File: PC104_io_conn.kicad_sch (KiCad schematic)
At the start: 8 parts, among them J1 ESQ-126-39-G-D, J2 ESQ-126-39-G-D

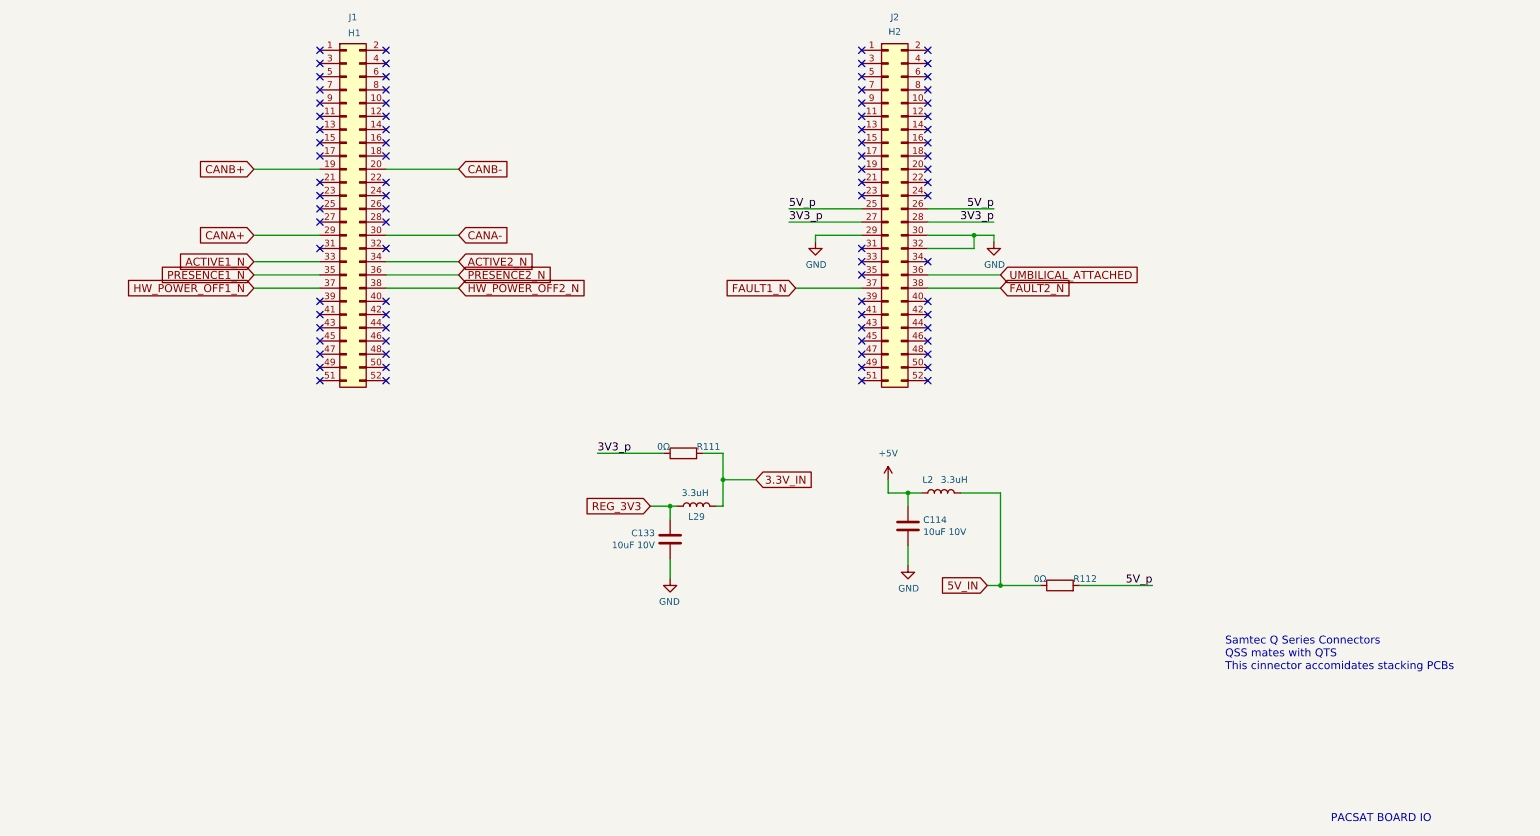
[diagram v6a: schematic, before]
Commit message: Add Power System Adapter function to the board
Signed-off-by: Corey Minyard <corey@minyard.net>
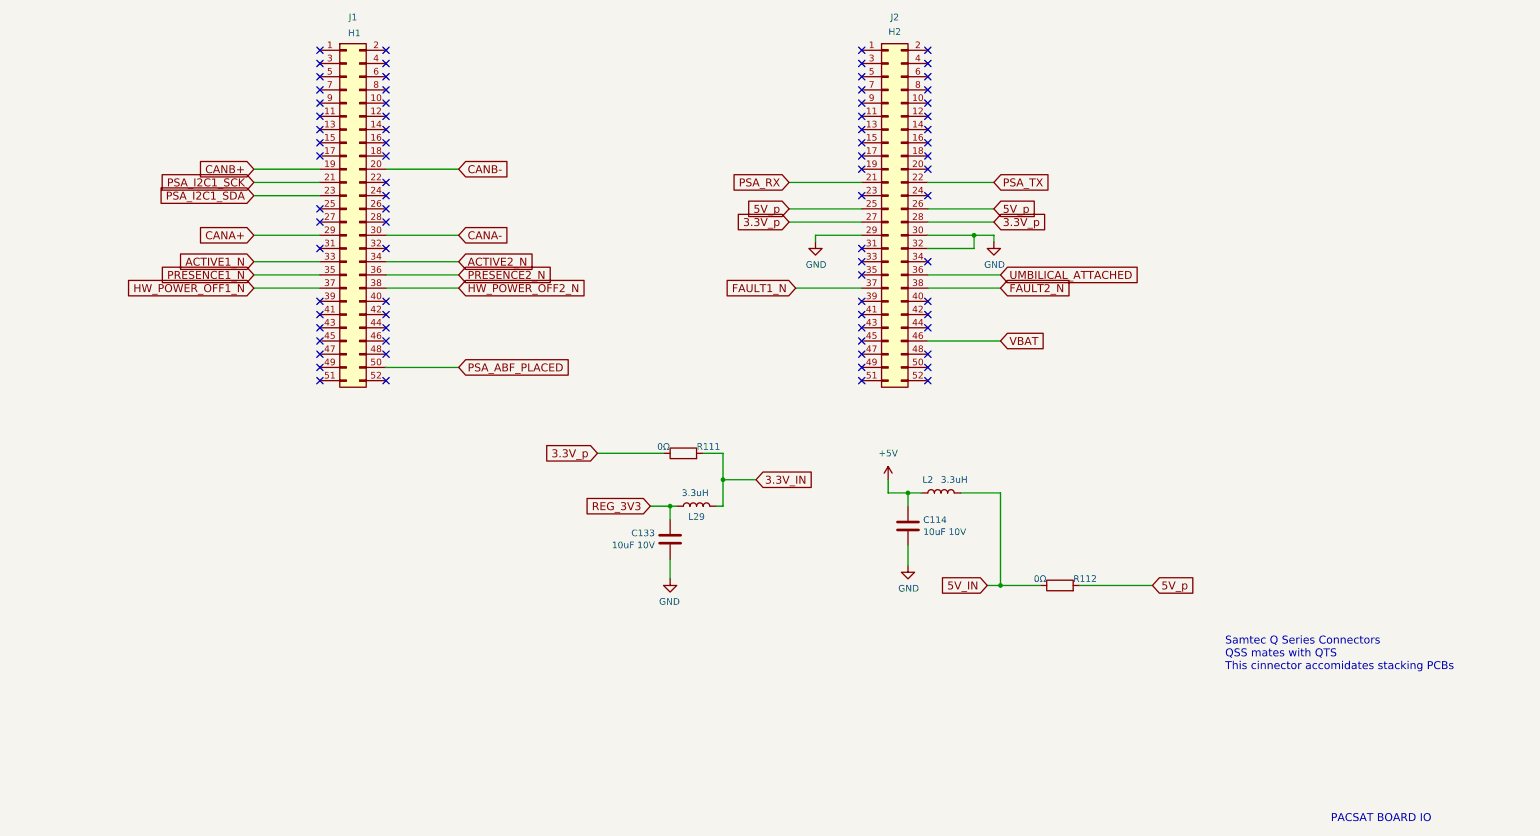
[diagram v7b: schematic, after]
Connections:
- net PSA_I2C1_SCK: now reaches J1.21 (Pin_21)
- net PSA_I2C1_SDA: now reaches J1.23 (Pin_23)
- net PSA_ABF_PLACED: now reaches J1.50 (Pin_50)
- net PSA_RX: now reaches J2.21 (Pin_21)
- net PSA_TX: now reaches J2.22 (Pin_22)
- net VBAT: now reaches J2.46 (Pin_46)
- net 3V3_p renamed 3.3V_p
- no-connect marks 84 -> 78

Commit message: Update the location and add a CSKB light connection
Move UMBILICAL_ATTACHED to the CSKB lite area, and add a SAFE\_MODE
pin to trigger the processor from another board to go into safe mode.

Signed-off-by: Corey Minyard <corey@minyard.net>
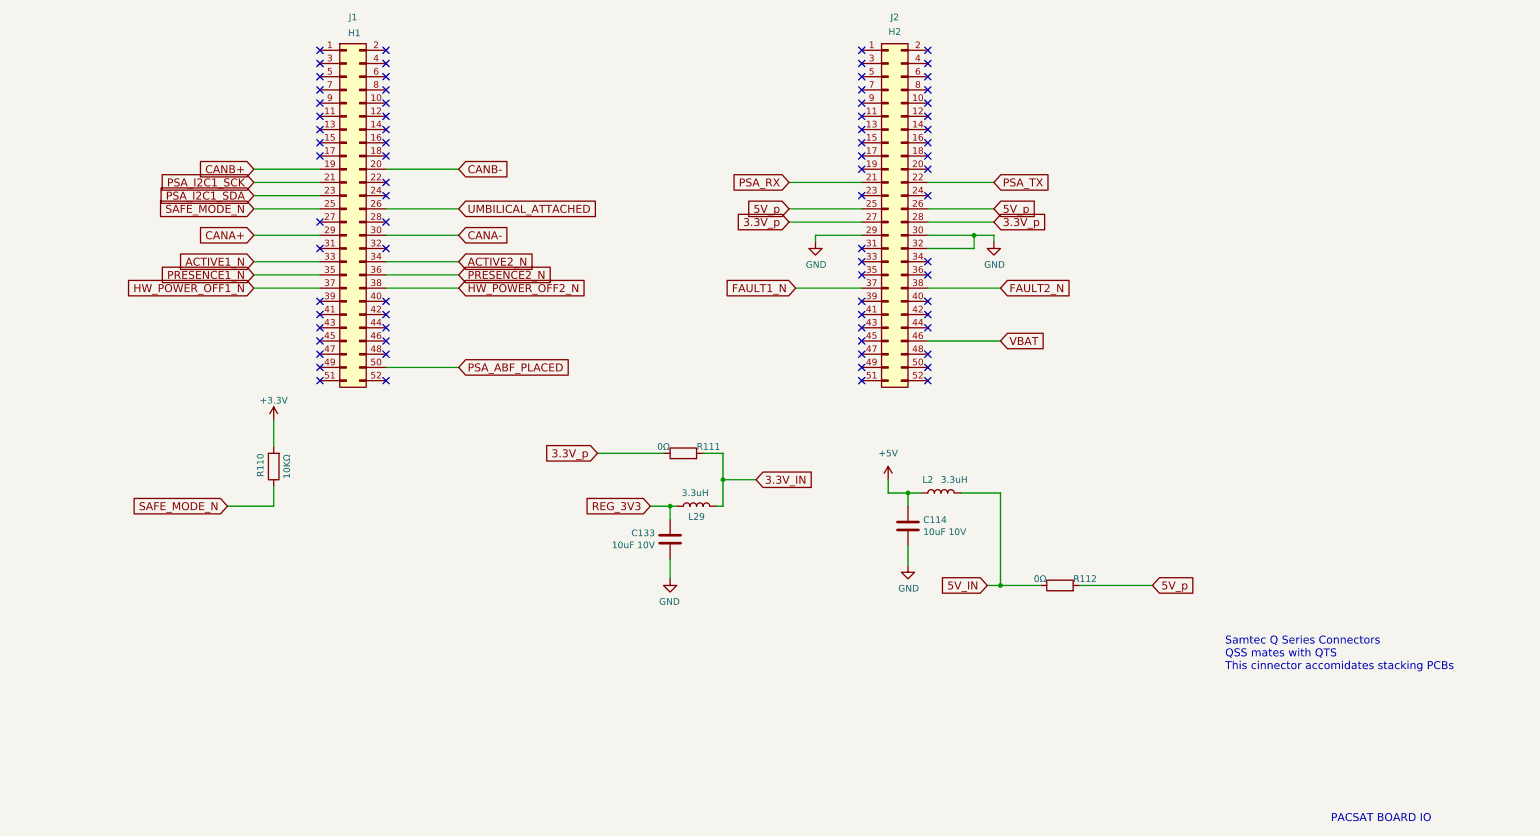
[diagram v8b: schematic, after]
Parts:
- added R110: 10KΩ, Resistor_SMD:R_0402_1005Metric_Pad0.72x0.64mm_HandSolder, symbol Device:R
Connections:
- net UMBILICAL_ATTACHED: now also J1.26 (Pin_26); no longer J2.36 (Pin_36)
- net SAFE_MODE_N: now reaches J1.25 (Pin_25)
- net SAFE_MODE_N: now also R110.1
- new net +3.3V: R110.2
- no-connect marks 78 -> 77
